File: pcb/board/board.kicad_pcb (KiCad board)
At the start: 2 copper layers, 56 x 80 mm, 137 parts, among them J1 (A) USB_C_Receptacle_USB2.0_1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, J10 OLED_128x32, J11 LCD_128x160, J12 AudioJack3, J13 Conn_01x01, J14 Micro_SD_Card, J15 Conn_01x01, J16 Conn_01x01, J17 Conn_01x01, J18 Conn_01x01, J19 Conn_01x01, J2 (B) USB_C_Receptacle_USB2.0_1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, J20 Conn_01x01, J21 Conn_01x01, J22 Conn_01x01, J3 (C) USB_C_Receptacle_USB2.0_1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, J6 Conn_01x01, J7 Conn_01x01, J8 Conn_01x01, J9 Conn_01x01, SW1 SW_Push, SW2 SW_Push, SW3 Switch, SW4 Switch, SW5 Switch, SW6 RotaryEncoder_Switch, U1 RP2040, U2 NCP1117-3.3_SOT223, U3 W25Q16JVZPIQ TR, U4 NCP1117-3.3_SOT223, U5 RP2040, U6 W25Q16JVZPIQ TR, U7 PCM5101A, U8 TLV70033_SOT23-5, U9 TPA6132A2RTE, Y1 12MHz, Y2 12MHz

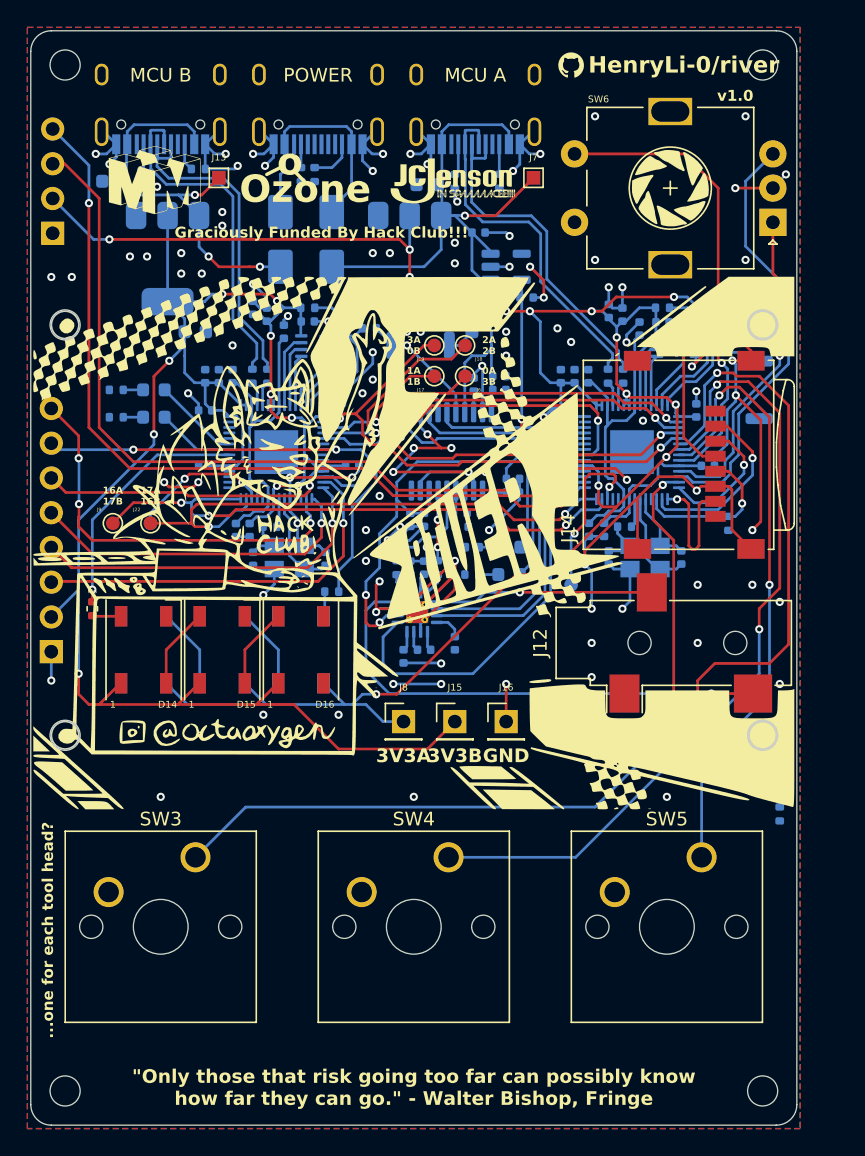
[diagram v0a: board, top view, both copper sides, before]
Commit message: audio jack moved to bottom layer!
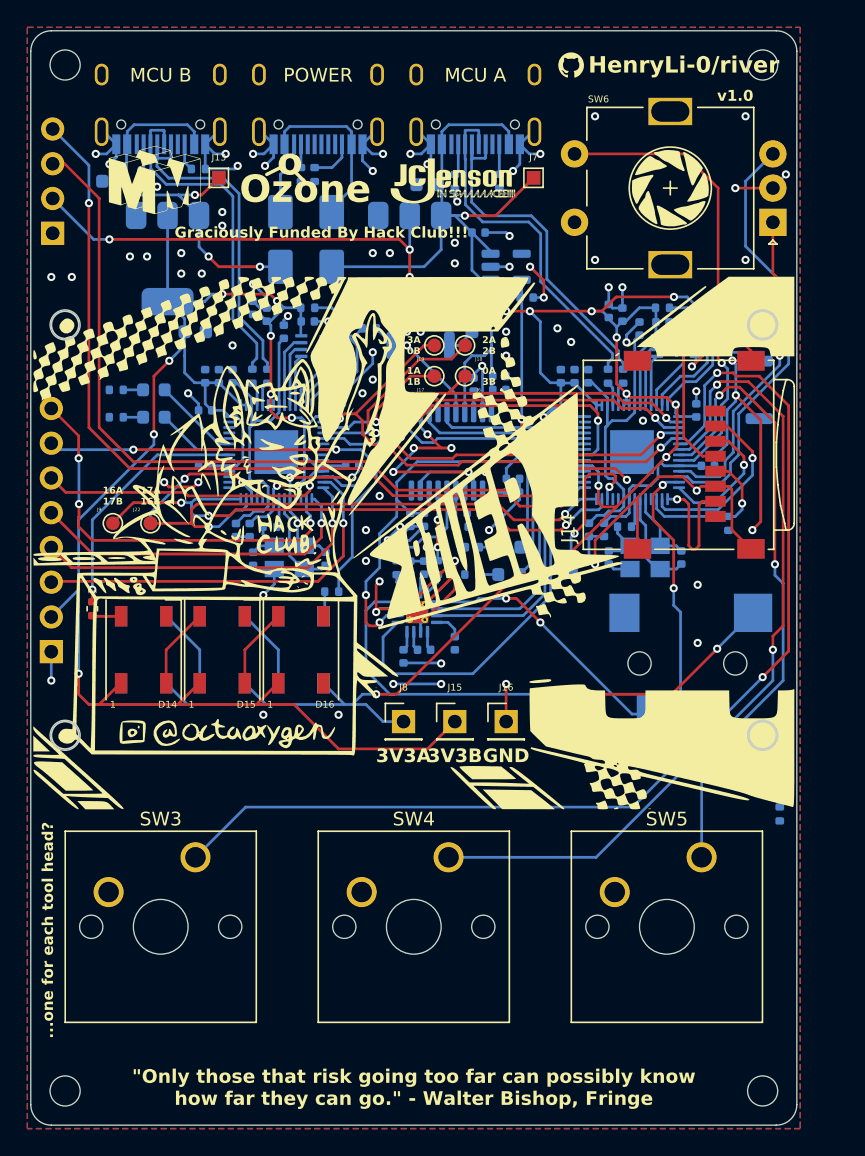
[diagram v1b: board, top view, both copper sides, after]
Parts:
- J12: moved to B.Cu
- moved G*** 72.9 mm to (88.3, 90.7)
- moved J12 1.50 mm to (147.0, 96.2), turned to -90 degrees
- moved J20 1.00 mm to (139.5, 89.5)
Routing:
- net GND: track 256.4 -> 250.4 mm, vias 114 -> 105
- net Net-(U9-OUTR): track 16.0 -> 19.3 mm, vias 1 -> 2
- net Net-(U9-OUTL): track 36.0 -> 38.4 mm, vias 1 -> 2
- net GPIO10_A: track 29.6 -> 28.3 mm, vias 2 -> 4
- net GPIO5_A: track 59.9 -> 61.0 mm
- net RUN_A: track 12.5 -> 11.5 mm
- net GPIO6_A: track 45.2 -> 46.0 mm
- net GPIO4_A: track 81.2 -> 80.4 mm

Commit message: micro sd card slot moved to bottom layer!
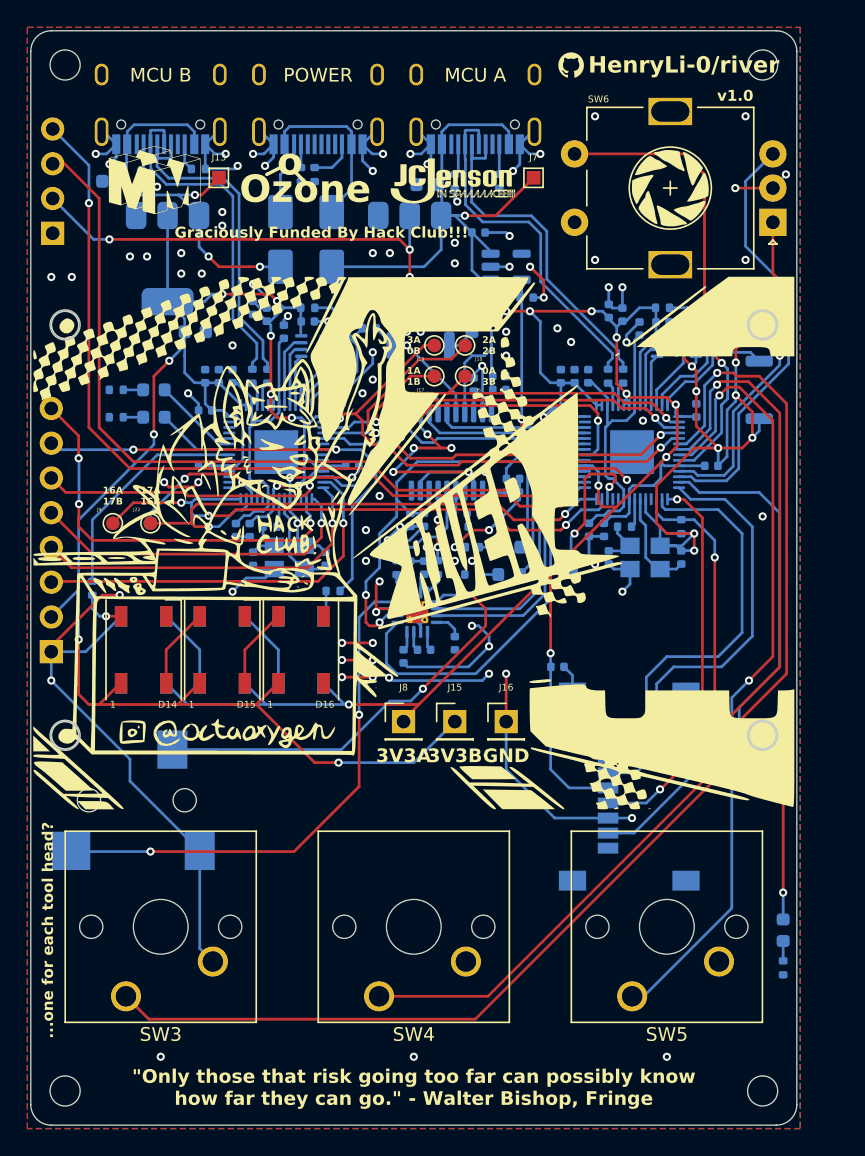
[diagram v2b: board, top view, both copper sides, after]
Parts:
- J14, R26: moved to B.Cu
- moved J12 39.5 mm to (108.8, 106.2), turned to 90 degrees
- moved C48 28.4 mm to (138.5, 96.5), turned to 0 degrees
- moved J14 24.7 mm to (143.8, 105.2)
- moved SW3 11.4 mm to (107.0, 120.6), turned to 180 degrees
- moved SW4 11.4 mm to (125.5, 120.6), turned to 180 degrees
- moved SW5 11.4 mm to (144.0, 120.6), turned to 180 degrees
- moved D5 11.3 mm to (155.0, 115.8)
- moved R24 11.3 mm to (155.0, 118.5)
- moved G*** 8.75 mm to (97.0, 90.7)
- moved R21 3.45 mm to (147.6, 86.2)
- moved R26 1.50 mm to (104.5, 90.8)
- moved C3 0.25 mm to (149.8, 81.8)
- moved R25 0.11 mm to (122.1, 91.0)
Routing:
- net GND: track 250.4 -> 311.0 mm, vias 105 -> 119
- net GPIO11_A: track 9.87 -> 32.2 mm, vias 1 -> 0
- net GPIO12_A: track 10.0 -> 30.1 mm, vias 1 -> 2
- net GPIO14_A: track 11.6 -> 30.2 mm, vias 1 -> 2
- net GPIO13_A: track 13.5 -> 31.0 mm, vias 1 -> 0
- net GPIO4_A: track 80.4 -> 93.3 mm, vias 2 -> 1
- net Net-(U9-OUTR): track 19.3 -> 32.1 mm
- net GPIO10_A: track 28.3 -> 40.6 mm, vias 4 -> 2
- net GPIO6_A: track 46.0 -> 58.1 mm
- net GPIO5_A: track 61.0 -> 71.4 mm, vias 2 -> 1
- net +3V3_A: track 193.4 -> 188.5 mm, vias 14 -> 13
- net GPIO23_B: track 18.0 -> 16.5 mm, vias 1 -> 0
- net Net-(D14-DIN): track 2.12 -> 3.32 mm, vias 0 -> 1
- net +3V3_B: track 138.9 -> 139.8 mm, vias 10 -> 11

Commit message: more ground vias and some silkscreen text fixes!
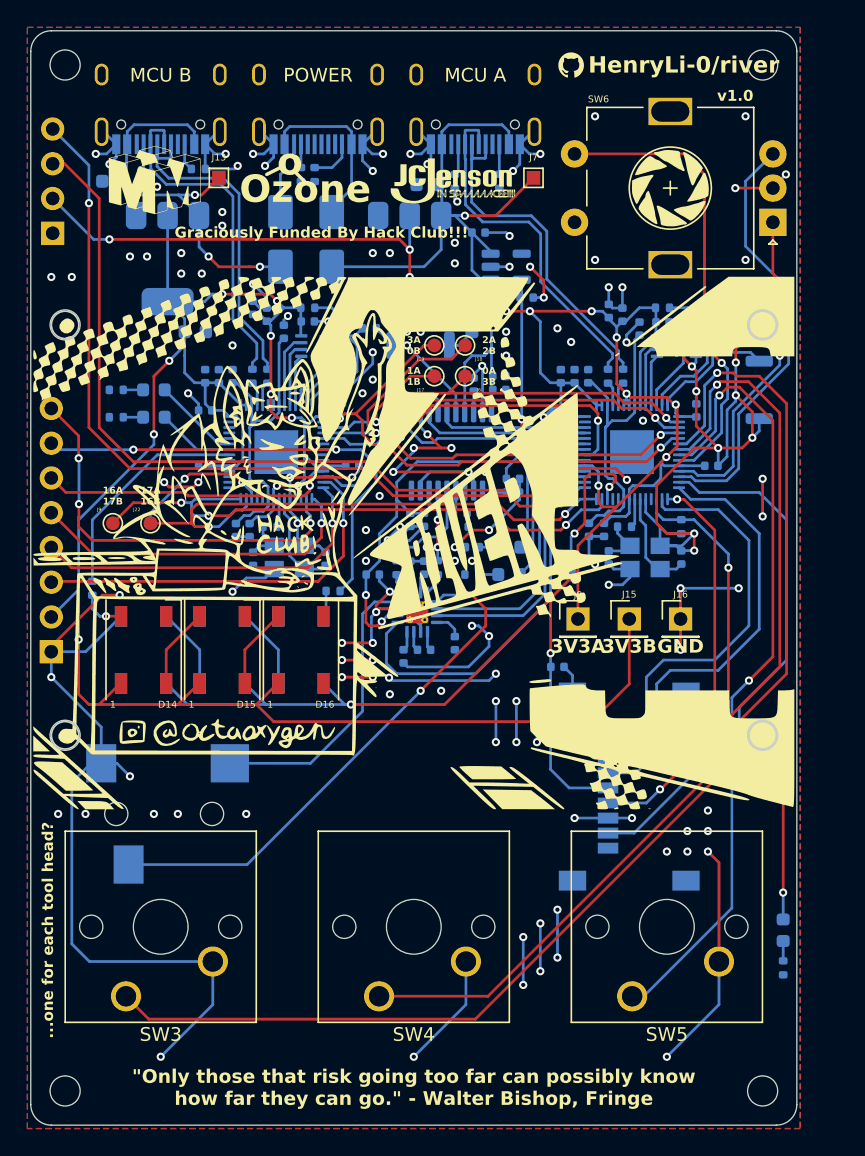
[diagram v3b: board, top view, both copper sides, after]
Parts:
- added C52: 2.2uF, Capacitor_SMD:C_0402_1005Metric, B.Cu at (125.0, 89.8)
- moved J15 14.8 mm to (143.8, 93.0)
- moved J16 14.8 mm to (147.5, 93.0)
- moved J8 14.8 mm to (140.0, 93.0)
- moved G*** 6.14 mm to (95.8, 96.8)
- moved J12 1.00 mm to (108.8, 107.2), turned to -90 degrees
- moved G*** 0.25 mm to (109.0, 89.0)
- moved J20 0.25 mm to (139.5, 89.8)
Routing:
- net GND: track 311.0 -> 377.1 mm, vias 119 -> 149
- net Net-(U9-OUTL): track 38.7 -> 21.3 mm, vias 2 -> 0
- net +3V3_B: track 139.8 -> 155.9 mm, vias 11 -> 10
- net Net-(U9-OUTR): track 32.1 -> 38.8 mm
- net +3V3_A: track 188.5 -> 189.4 mm
- net GPIO14_A: track 30.2 -> 31.0 mm
- net GPIO12_A: track 30.1 -> 30.9 mm

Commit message: lots of silkscreen and art fixes!
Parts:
- moved G*** 66.4 mm to (161.2, 107.5)
- moved J15 3.78 mm to (147.5, 92.5)
- moved J16 3.78 mm to (151.2, 92.5)
- moved J8 3.78 mm to (143.8, 92.5)
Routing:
- net GND: track 377.1 -> 383.3 mm, vias 149 -> 152
- net +3V3_A: track 189.4 -> 193.7 mm
- net +3V3_B: track 155.9 -> 159.1 mm
- net GPIO13_A: track 31.4 -> 33.9 mm
- net GPIO11_A: track 32.6 -> 34.8 mm
- net GPIO12_A: track 30.9 -> 32.9 mm
- net GPIO14_A: track 31.0 -> 32.8 mm
- net GPIO10_A: vias 2 -> 0
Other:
- board text added: "Made with lots of <3 by henry with Hack Club! :3"
- board text added: "music data!"
- board text added: "secret way :o"
